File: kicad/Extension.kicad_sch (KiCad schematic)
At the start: 23 parts, among them J1 FLE-126-01-G-DV, SW1 PTS645SK43SMTR92 LFS

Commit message: Changed the name of the project path to ECP5_BGA381_FT2232HQ_FIFO_EXT
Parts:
- J1: footprint ECP5_TX_AUDIO_EXT:SAMTEC_FLE-126-01-G-DV -> ECP5_BGA381_FT2232HQ_FIFO_EXT:SAMTEC_FLE-126-01-G-DV
- TP1, TP2, TP3, TP4, TP5: footprint ECP5_TX_AUDIO_EXT:KEYSTONE_5197TR -> ECP5_BGA381_FT2232HQ_FIFO_EXT:KEYSTONE_5197TR
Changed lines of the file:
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@@
 			)
 		)
-		(property "Footprint" "ECP5_TX_AUDIO_EXT:KEYSTONE_5197TR"
+		(property "Footprint" "ECP5_BGA381_FT2232HQ_FIFO_EXT:KEYSTONE_5197TR"
 			(at 27.94 179.07 0)
 			(effects
@@
 			)
 		)
-		(property "Footprint" "ECP5_TX_AUDIO_EXT:SAMTEC_FLE-126-01-G-DV"
+		(property "Footprint" "ECP5_BGA381_FT2232HQ_FIFO_EXT:SAMTEC_FLE-126-01-G-DV"
 			(at 261.62 87.63 0)
 			(effects
@@
 			)
 		)
-		(property "Footprint" "ECP5_TX_AUDIO_EXT:KEYSTONE_5197TR"
+		(property "Footprint" "ECP5_BGA381_FT2232HQ_FIFO_EXT:KEYSTONE_5197TR"
 			(at 43.18 179.07 0)
 			(effects
@@
 			)
 		)
-		(property "Footprint" "ECP5_TX_AUDIO_EXT:KEYSTONE_5197TR"
+		(property "Footprint" "ECP5_BGA381_FT2232HQ_FIFO_EXT:KEYSTONE_5197TR"
 			(at 57.15 179.07 0)
 			(effects
@@
 			)
 		)
-		(property "Footprint" "ECP5_TX_AUDIO_EXT:KEYSTONE_5197TR"
+		(property "Footprint" "ECP5_BGA381_FT2232HQ_FIFO_EXT:KEYSTONE_5197TR"
 			(at 71.12 179.07 0)
 			(effects
@@
 			)
 		)
-		(property "Footprint" "ECP5_TX_AUDIO_EXT:KEYSTONE_5197TR"
+		(property "Footprint" "ECP5_BGA381_FT2232HQ_FIFO_EXT:KEYSTONE_5197TR"
 			(at 86.36 179.07 0)
 			(effects

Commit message: First pass at arranging components
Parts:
- added C1, C2, C5: 0.1µF, Capacitor_SMD:C_0603_1608Metric, symbol Device:C_Small
- added C3, C7: 4.7µF, Capacitor_SMD:C_0603_1608Metric, symbol Device:C_Small
- added C4: 18nF, Capacitor_SMD:C_0603_1608Metric, symbol Device:C_Small
- added C6: 10µF, Capacitor_SMD:C_0805_2012Metric, symbol Device:C_Small
- added D10, D11, D12, D19, D25, D9: BLUE, LED_SMD:LED_0603_1608Metric, symbol Device:LED
- added D13, D14, D15, D16, D18, D22, D24: GREEN, LED_SMD:LED_0603_1608Metric, symbol Device:LED
- added D17, D21, D23: YELLOW, LED_SMD:LED_0603_1608Metric, symbol Device:LED
- added D20: RED, LED_SMD:LED_0603_1608Metric, symbol Device:LED
- added J2: RCJ-044, ECP5_BGA381_FT2232HQ_FIFO_EXT:CUI_RCJ-042, symbol ECP5_BGA381_FT2232HQ_FIFO_EXT:Conn_Coaxial
- added J3: HDMI_A, ECP5_BGA381_FT2232HQ_FIFO_EXT:AMPHENOL_10029449-001RLF, symbol Connector:HDMI_A
- added L1: 1µH, Inductor_SMD:L_Coilcraft_XxL4040, symbol Device:L
- added R10, R11, R12, R13, R14, R15, R16, R18, R22, R24, R3, R4, R9: 330, Resistor_SMD:R_0603_1608Metric, symbol Device:R_US
- added R17, R20, R21, R23: 750, Resistor_SMD:R_0603_1608Metric, symbol Device:R_US
- added R26: 150, Resistor_SMD:R_0603_1608Metric, symbol Device:R_US
- added R28: 75, Resistor_SMD:R_0603_1608Metric, symbol Device:R_US
- added TP5, TP6: 5190TR, ECP5_BGA381_FT2232HQ_FIFO_EXT:KEYSTONE_5197TR, symbol Connector:TestPoint
- added U1: 74HC04, Package_SO:TSSOP-14_4.4x5mm_P0.65mm, symbol 74xx:74HC04
- added U2: TPS22948, Package_TO_SOT_SMD:SOT-363_SC-70-6, symbol ECP5_BGA381_FT2232HQ_FIFO_EXT:TPS22948
- added U3: DSLVDS1047, ECP5_BGA381_FT2232HQ_FIFO_EXT:TSSOP-16-1EP_4.4x5mm_P0.65mm, symbol ECP5_BGA381_FT2232HQ_FIFO_EXT:DSLVDS1047
- added U4: TPS610333, ECP5_BGA381_FT2232HQ_FIFO_EXT:SOT-583-8, symbol ECP5_BGA381_FT2232HQ_FIFO_EXT:TPS61033
- D1, D2: value YELLOW -> BLUE; MPN APT1608LSYCK/J3-PRV -> APT1608LVBC/D
- D3, D4: value GREEN -> BLUE; MPN APT1608LZGCK -> APT1608LVBC/D
- D5, D6: value RED -> BLUE; MPN APT1608LSECK/J3-PRV -> APT1608LVBC/D
- R1, R2, R5, R6: value 750 -> 330; MPN ERJ-3EKF7500V -> ERJ-3EKF3300V
- TP1: value 5190TR -> 51907R; MPN 5190TR -> 5197TR
- TP2: value 5190TR -> 5197TR; MPN 5190TR -> 5197TR
- TP7: renamed from TP5; value 5197TR -> 5191TR; MPN 5197TR -> 51971R
- renumbered R3 to R19, R4 to R25
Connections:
- net +3V3: now also C1.1, C5.1, C7.1, L1.1, U1.14 (VCC), U3.1 (EN), U3.4 (VCC), U4.1 (VIN), U4.2 (EN), U4.3 (MODE), U4.5 (FB)
- net EXT_1: now also TP1.1; no longer TP4.1
- net EXT_10: now also TP5.1, U3.6 (DIN3)
- net EXT_12: now also TP6.1, U3.7 (DIN4)
- net EXT_14: now also D13.2 (A)
- net EXT_16: now also D14.2 (A)
- net EXT_18: now also D12.2 (A)
- net EXT_2: now also TP2.1; no longer TP3.1
- net EXT_20: now also D11.2 (A)
- net EXT_22: now also D10.2 (A)
- net EXT_24: now also D9.2 (A)
- net EXT_26: now also D8.2 (A)
- net EXT_28: now also D7.2 (A)
- net EXT_29: now also D20.2 (A)
- net EXT_30: now also D6.2 (A)
- net EXT_31: now also D19.2 (A)
- net EXT_32: now also D5.2 (A)
- net EXT_33: now also D25.2 (A)
- net EXT_34: now also D4.2 (A)
- net EXT_35: now also D18.2 (A)
- net EXT_36: now also D3.2 (A)
- net EXT_37: now also D23.2 (A)
- net EXT_38: now also D2.2 (A); no longer D8.2 (A)
- net EXT_39: now also D17.2 (A); no longer D7.2 (A)
- net EXT_4: now also U1.1; no longer TP1.1
- net EXT_40: now also D1.2 (A); no longer D6.2 (A)
- net EXT_41: now also D24.2 (A); no longer D5.2 (A)
- net EXT_42: now also D16.2 (A); no longer D4.2 (A)
- net EXT_43: now also D22.2 (A); no longer D3.2 (A)
- net EXT_44: now also D15.2 (A); no longer D2.2 (A)
- net EXT_45: now also D21.2 (A); no longer D1.2 (A)
- net EXT_6: now also TP3.1, U3.2 (DIN1)
- net EXT_8: now also TP4.1, U3.3 (DIN2)
- net GND: now also C1.2, C3.2, C4.2, C5.2, C6.2, C7.2, J2.1 (Ext), J3.11 (CKS), J3.17 (GND), J3.2 (D2S), J3.5 (D1S), J3.8 (D0S), J3.SH, R10.2, R11.2, R12.2, R13.2, R14.2, R15.2, R16.2, R17.2, R18.2, R20.2, R21.2, R22.2, R23.2, R24.2, R28.2, R3.2, R4.2, R9.2, U1.11, U1.13, U1.7 (GND), U1.9, U2.2 (GND), U3.5 (GND), U3.8 (~{EN}), U4.6 (GND)
- net at R25.1: now also D25.1 (K); no longer D4.1 (K)
- net at D3.1 (K): now also R3.1; no longer R19.1
- net EXT_11: no longer names the net of J1.37 (Pin_37)
- net EXT_13: no longer names the net of J1.35 (Pin_35)
- net EXT_15: no longer names the net of J1.33 (Pin_33)
- net EXT_17: no longer names the net of J1.31 (Pin_31)
- net EXT_19: no longer names the net of J1.29 (Pin_29)
- net EXT_21: no longer names the net of J1.27 (Pin_27)
- net EXT_23: no longer names the net of J1.25 (Pin_25)
- net EXT_25: no longer names the net of J1.23 (Pin_23)
- net EXT_27: no longer names the net of J1.21 (Pin_21)
- net EXT_3: no longer names the net of J1.45 (Pin_45)
- net EXT_3: no longer TP2.1
- net EXT_5: no longer names the net of J1.43 (Pin_43)
- net EXT_7: no longer names the net of J1.41 (Pin_41)
- net EXT_9: no longer names the net of J1.39 (Pin_39)
- new net: D18.1 (K), R18.1
- new net: D14.1 (K), R14.1
- new net: D15.1 (K), R15.1
- new net: D13.1 (K), R13.1
- new net: D9.1 (K), R9.1
- new net: L1.2, U4.7 (SW)
- new net: D11.1 (K), R11.1
- new net: D24.1 (K), R24.1
- new net: C4.1, J3.18 (+5V), U2.6 (VOUT)
- new net: C2.1, J2.2 (In)
- new net: U1.2, U1.3, U1.5
- new net: R26.2, U1.4, U1.6
- new net: D20.1 (K), R20.1
- new net: C2.2, R26.1, R28.1
- new net: D17.1 (K), R17.1
- new net: D4.1 (K), R4.1
- new net: D21.1 (K), R21.1
- new net: D22.1 (K), R22.1
- new net: D19.1 (K), R19.1
- new net: D10.1 (K), R10.1
- new net: D23.1 (K), R23.1
- new net: D16.1 (K), R16.1
- new net: D12.1 (K), R12.1
- new net +5V: C3.1, C6.1, U2.1 (VIN), U2.3 (ON), U4.8 (VOUT)
- new net DIFF_BCLK+: J3.4 (D1+), U3.14 (DOUT2+)
- new net DIFF_BCLK-: J3.6 (D1-), U3.13 (DOUT2-)
- new net DIFF_LRCK+: J3.7 (D0+), U3.11 (DOUT3+)
- new net DIFF_LRCK-: J3.9 (D0-), U3.12 (DOUT3-)
- new net DIFF_MCLK+: J3.10 (CK+), U3.10 (DOUT4+)
- new net DIFF_MCLK-: J3.12 (CK-), U3.9 (DOUT4-)
- new net DIFF_SDATA+: J3.1 (D2+), U3.15 (DOUT1+)
- new net DIFF_SDATA-: J3.3 (D2-), U3.16 (DOUT1-)
- no-connect marks 0 -> 23
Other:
- note added: "0.5 Vpp Max. 0.6 Vpp"
- note added: "0.55 Vpp"
- note added: "16-bit"
- note added: "176.4KHZ"
- note added: "192KHZ"
- note added: "24-bit"
- note added: "32-bit"
- note added: "352.8KHZ"
- note added: "384KHZ"
- note added: "44.1KHZ"
- note added: "48KHZ"
- note added: "88.2KHZ"
- note added: "96KHZ"
- note added: "BCLK"
- note added: "Button"
- note added: "CTRL ERROR"
- note added: "CTRL TP 1"
- note added: "CTRL TP 2"
- note added: "Connector"
- note added: "DoP"
- note added: "Extension for the ECP5 & FT2232HQ Audio Board"
- note added: "FT2232 FIFO HAS DATA"
- note added: "FT2232 IN FIFO FULL"
- note added: "GND"
- note added: "HDMI"
- note added: "I2S STREAMING"
- note added: "IN FIFO DATA"
- note added: "IN FIFO FULL"
- note added: "IN FIFO RD"
- note added: "LEDs"
- note added: "LRCK"
- note added: "MCLK"
- note added: "OUT FIFO DATA"
- note added: "OUT FIFO FULL"
- note added: "OUT FIFO WR"
- note added: "PWM mode"
- note added: "RCA"
- note added: "RD FT2232 DATA"
- note added: "SDATA"
- note added: "SPDIF STREAMING"
- note added: "Test Points"
- note added: "WR FT2232 IN FIFO"
- note removed: "ALT_INT"
- note removed: "Extension for the USB Audio Board"
- note removed: "ID"
- note removed: "LINESTATE [1:0]"
- note removed: "RxEvent [5:4]"
- note removed: "VBUS State [3:2]"
- moved on the sheet: J1, R19, R25, SW1, TP1, TP2, TP3, TP4, TP7

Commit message: Updated the BOM
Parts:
- added TP8: 5191TR, ECP5_BGA381_FT2232HQ_FIFO_EXT:KEYSTONE_5197TR, symbol Connector:TestPoint
- J3: value HDMI_A -> HDMI A
- TP1: value 51907R -> 5197TR
- TP7: MPN 51971R -> 5191TR
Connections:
- net GND: now also TP8.1

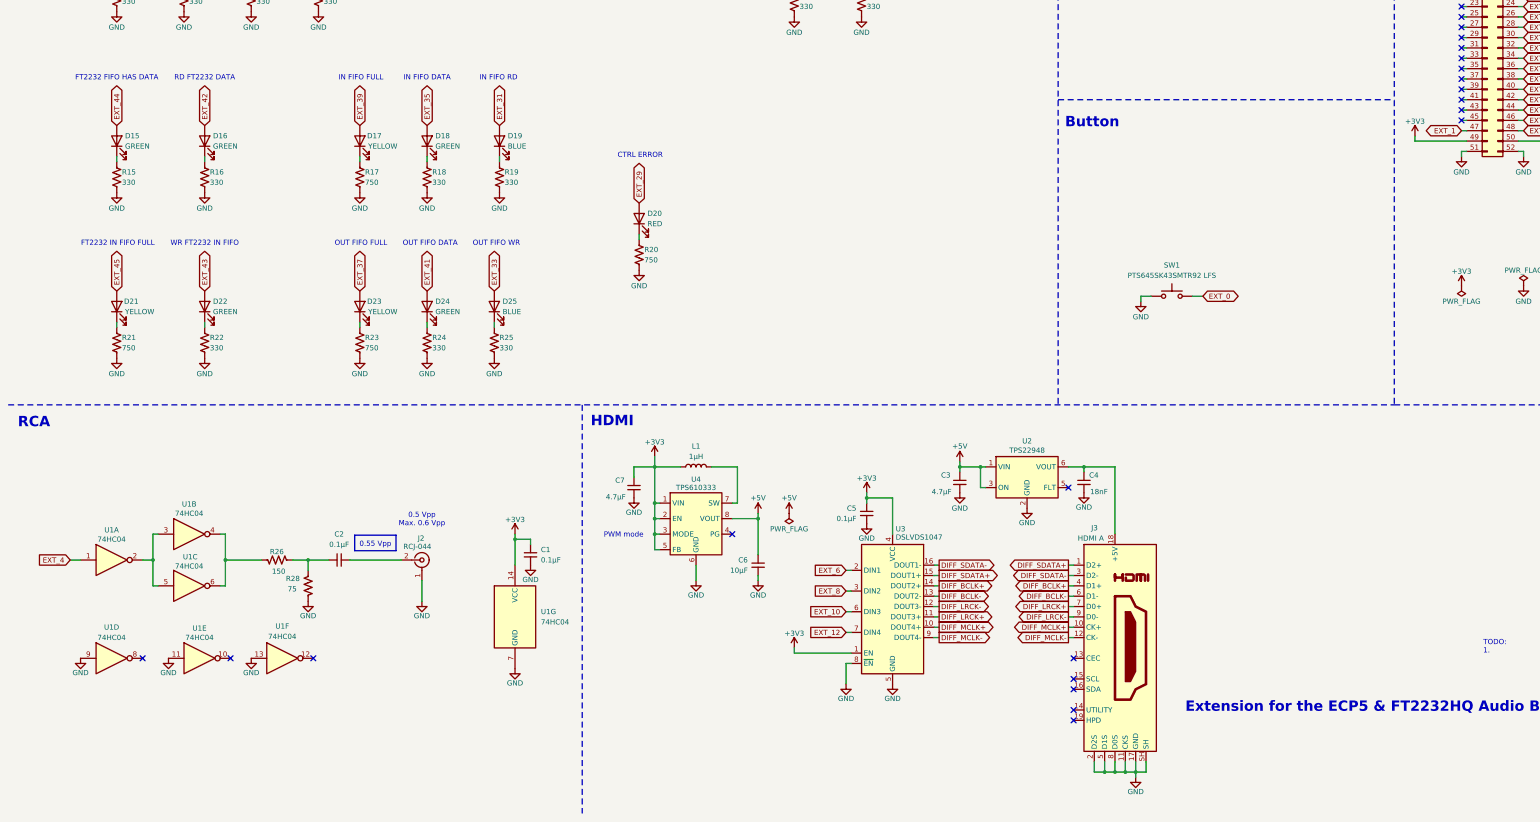
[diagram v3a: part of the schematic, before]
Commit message: Removed unused symbols and footprints
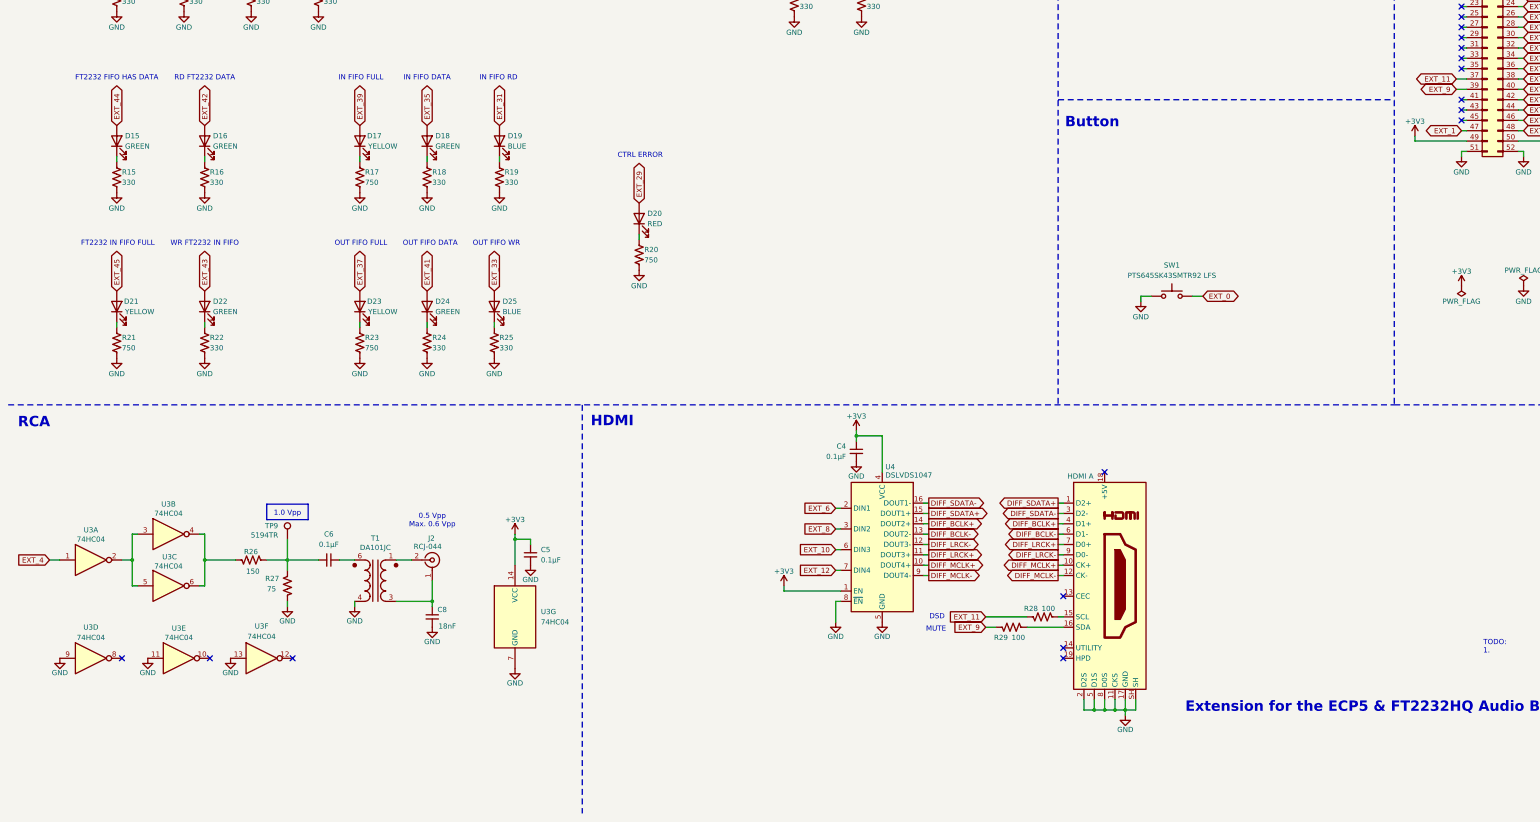
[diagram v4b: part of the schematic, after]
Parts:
- removed C3, C7: 4.7µF, Capacitor_SMD:C_0603_1608Metric, symbol Device:C_Small
- removed C4: 18nF, Capacitor_SMD:C_0603_1608Metric, symbol Device:C_Small
- removed C6: 10µF, Capacitor_SMD:C_0805_2012Metric, symbol Device:C_Small
- removed L1: 1µH, Inductor_SMD:L_Coilcraft_XxL4040, symbol Device:L
- removed U2: TPS22948, Package_TO_SOT_SMD:SOT-363_SC-70-6, symbol ECP5_BGA381_FT2232HQ_FIFO_EXT:TPS22948
- removed U4: TPS610333, ECP5_BGA381_FT2232HQ_FIFO_EXT:SOT-583-8, symbol ECP5_BGA381_FT2232HQ_FIFO_EXT:TPS61033
- added C8: 18nF, Capacitor_SMD:C_0603_1608Metric, symbol Device:C_Small
- added R28, R29: 100, Resistor_SMD:R_0603_1608Metric, symbol Device:R_US
- added T1: DA101JC, ECP5_BGA381_FT2232HQ_FIFO_EXT:DA101J_MUR, symbol ECP5_BGA381_FT2232HQ_FIFO_EXT:Transformer_1P_1S
- added TP9: 5194TR, ECP5_BGA381_FT2232HQ_FIFO_EXT:KEYSTONE_5197TR, symbol Connector:TestPoint
- renumbered C5 to C4, C1 to C5, C2 to C6, R28 to R27, U1 to U3, U3 to U4
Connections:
- net GND: now also C8.2, T1.4 (SA); no longer J2.1 (Ext)
- net EXT_11: now reaches J1.37 (Pin_37)
- net EXT_11: now also R28.2
- net EXT_9: now reaches J1.39 (Pin_39)
- net EXT_9: now also R29.2
- net at J2.2 (In): now also T1.1 (AA); no longer C6.1
- net at C6.2, R26.1, R27.1: now also TP9.1
- net at J3.15 (SCL): now also R28.1
- net at J3.16 (SDA): now also R29.1
- new net: C8.1, J2.1 (Ext), T1.3 (AB)
- new net: C6.1, T1.6 (SB)
- no-connect marks 23 -> 18
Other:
- note added: "1.0 Vpp"
- note added: "DSD"
- note added: "MUTE"
- note removed: "0.55 Vpp"
- note removed: "PWM mode"
- moved on the sheet: C4, C6, J2, R26, R27, U3A, U3B, U3C, U3D, U3E, U3F, U4

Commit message: First routing
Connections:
- net EXT_10: now also TP4.1, U4.3 (DIN2); no longer TP5.1, U4.6 (DIN3)
- net EXT_12: now also TP3.1, U4.2 (DIN1); no longer TP6.1, U4.7 (DIN4)
- net EXT_6: now also TP6.1, U4.7 (DIN4); no longer TP3.1, U4.2 (DIN1)
- net EXT_8: now also TP5.1, U4.6 (DIN3); no longer TP4.1, U4.3 (DIN2)
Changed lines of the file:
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@@
 		)
 	)
-	(global_label "EXT_8"
+	(global_label "EXT_10"
 		(shape bidirectional)
 		(at 306.07 54.61 270)
@@
 		)
 		(property "Intersheetrefs" "${INTERSHEET_REFS}"
-			(at 306.07 64.2097 90)
+			(at 306.07 65.4192 90)
 			(effects
 				(font
@@
 		)
 	)
-	(global_label "EXT_6"
+	(global_label "EXT_12"
 		(shape bidirectional)
 		(at 292.1 54.61 270)
@@
 		)
 		(property "Intersheetrefs" "${INTERSHEET_REFS}"
-			(at 292.1 64.2097 90)
+			(at 292.1 65.4192 90)
 			(effects
 				(font
@@
 		)
 	)
-	(global_label "EXT_10"
+	(global_label "EXT_8"
 		(shape bidirectional)
 		(at 321.31 54.61 270)
@@
 		)
 		(property "Intersheetrefs" "${INTERSHEET_REFS}"
-			(at 321.31 65.4192 90)
+			(at 321.31 64.2097 90)
 			(effects
 				(font
@@
 		)
 	)
-	(global_label "EXT_12"
+	(global_label "EXT_6"
 		(shape bidirectional)
 		(at 336.55 54.61 270)
@@
 		)
 		(property "Intersheetrefs" "${INTERSHEET_REFS}"
-			(at 336.55 65.4192 90)
+			(at 336.55 64.2097 90)
 			(effects
 				(font
@@
 		)
 	)
-	(global_label "EXT_10"
+	(global_label "EXT_8"
 		(shape input)
 		(at 215.9 219.71 180)
@@
 		)
 		(property "Intersheetrefs" "${INTERSHEET_REFS}"
-			(at 206.2021 219.71 0)
+			(at 207.4116 219.71 0)
 			(effects
 				(font
@@
 		)
 	)
-	(global_label "EXT_6"
+	(global_label "EXT_12"
 		(shape input)
 		(at 215.9 209.55 180)
@@
 		)
 		(property "Intersheetrefs" "${INTERSHEET_REFS}"
-			(at 207.4116 209.55 0)
+			(at 206.2021 209.55 0)
 			(effects
 				(font
@@
 		)
 	)
-	(global_label "EXT_12"
+	(global_label "EXT_6"
 		(shape input)
 		(at 215.9 224.79 180)
@@
 		)
 		(property "Intersheetrefs" "${INTERSHEET_REFS}"
-			(at 206.2021 224.79 0)
-			(effects
-				(font
-					(size 1.27 1.27)
-				)
-				(justify right)
-				(hide yes)
-			)
-		)
-	)
-	(global_label "EXT_8"
+			(at 207.4116 224.79 0)
+			(effects
+				(font
+					(size 1.27 1.27)
+				)
+				(justify right)
+				(hide yes)
+			)
+		)
+	)
+	(global_label "EXT_10"
 		(shape input)
 		(at 215.9 214.63 180)
@@
 		)
 		(property "Intersheetrefs" "${INTERSHEET_REFS}"
-			(at 207.4116 214.63 0)
-			(effects
-				(font
+			(at 206.2021 214.63 0)
+			(effects
+				(font
